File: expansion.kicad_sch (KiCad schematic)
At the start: 41 parts, among them IC10 GAL16V8, IC11 74LS367ADR, IC12 74LS367ADR, IC13 74LS368AD, IC14 74LS367ADR, IC15 74ALS30ADR, IC16 74LS245DWR, IC17 74LS367ADR, IC18 74LS139ADR, IC19 74LS153DR, IC20 74LS374DWR, IC21 74LS367ADR, IC22 74LS74ADR, J10 CARTRIDGE EDGE, J12 CARTRIDGE EDGE, J13 CARTRIDGE EDGE, J9 CARTRIDGE EDGE, SW3 DEFAULT SLOT

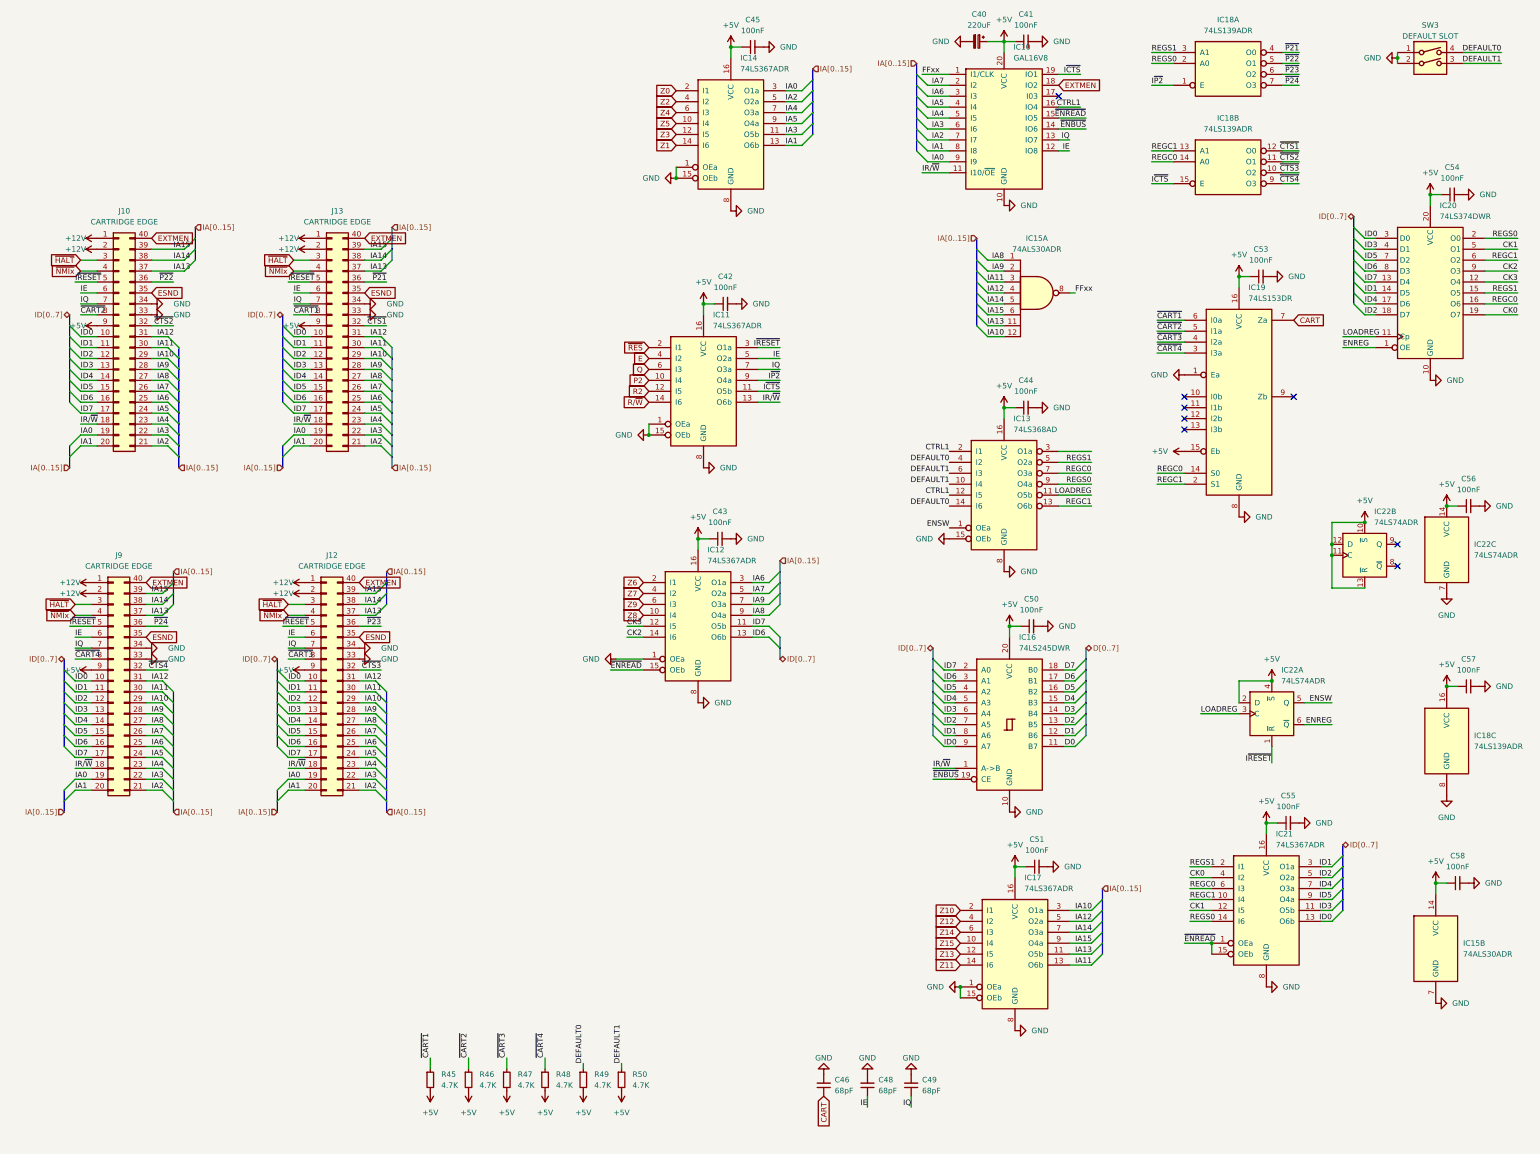
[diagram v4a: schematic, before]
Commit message: add data bus transceiver
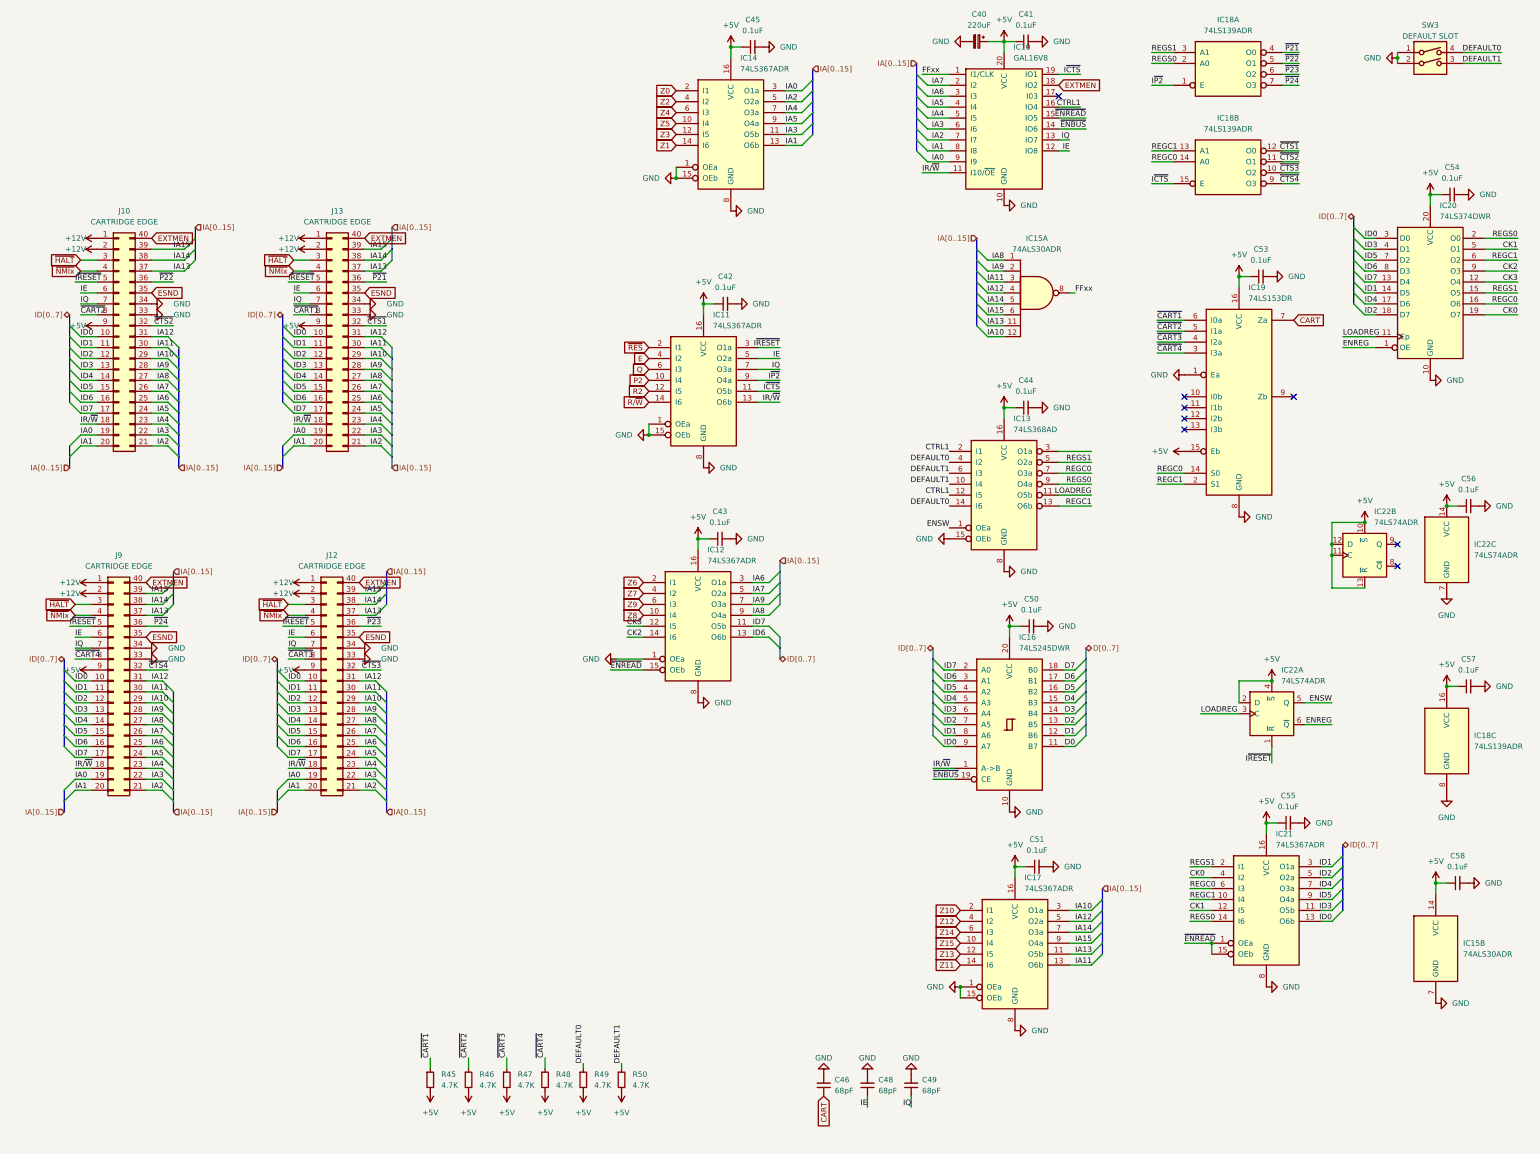
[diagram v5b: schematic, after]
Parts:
- C40: DigiKey (none) -> 732-875575345004CT-ND
- C41, C42, C43, C44, C45, C50, C51, C53, C54, C55, C56, C57, C58: value 100nF -> 0.1uF; DigiKey (none) -> 399-C0805C104K4RAC7800CT-ND
- C46, C48, C49: DigiKey (none) -> 399-C0805C680J5GAC7800CT-ND
- R45, R46, R47, R48, R49, R50: DigiKey (none) -> 541-4131-1-ND
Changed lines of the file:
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@@
 			)
 		)
-		(property "Value" "100nF"
+		(property "Value" "0.1uF"
 			(at 347.9863 201.93 90)
 			(effects
@@
 			)
 		)
+		(property "DigiKey" "399-C0805C104K4RAC7800CT-ND"
+			(at 347.98 205.74 90)
+			(effects
+				(font
+					(size 1.27 1.27)
+				)
+				(hide yes)
+			)
+		)
 		(pin "1"
 		)
@@
 			)
 		)
-		(property "Value" "100nF"
+		(property "Value" "0.1uF"
 			(at 389.8963 170.18 90)
 			(effects
@@
 			)
 		)
+		(property "DigiKey" "399-C0805C104K4RAC7800CT-ND"
+			(at 389.89 173.99 90)
+			(effects
+				(font
+					(size 1.27 1.27)
+				)
+				(hide yes)
+			)
+		)
 		(pin "1"
 		)
@@
 			)
 		)
-		(property "Value" "100nF"
+		(property "Value" "0.1uF"
 			(at 387.3563 215.9 90)
 			(effects
@@
 			)
 		)
+		(property "DigiKey" "399-C0805C104K4RAC7800CT-ND"
+			(at 387.35 219.71 90)
+			(effects
+				(font
+					(size 1.27 1.27)
+				)
+				(hide yes)
+			)
+		)
 		(pin "1"
 		)
@@
 			)
 		)
+		(property "DigiKey" "399-C0805C680J5GAC7800CT-ND"
+			(at 250.19 266.7 0)
+			(effects
+				(font
+					(size 1.27 1.27)
+				)
+				(hide yes)
+			)
+		)
 		(pin "1"
 		)
@@
 			)
 		)
-		(property "Value" "100nF"
+		(property "Value" "0.1uF"
 			(at 217.1763 81.28 90)
 			(effects
@@
 			)
 		)
+		(property "DigiKey" "399-C0805C104K4RAC7800CT-ND"
+			(at 217.17 85.09 90)
+			(effects
+				(font
+					(size 1.27 1.27)
+				)
+				(hide yes)
+			)
+		)
 		(pin "1"
 		)
@@
 			)
 		)
-		(property "Value" "100nF"
+		(property "Value" "0.1uF"
 			(at 389.8963 128.27 90)
 			(effects
@@
 			)
 		)
+		(property "DigiKey" "399-C0805C104K4RAC7800CT-ND"
+			(at 389.89 132.08 90)
+			(effects
+				(font
+					(size 1.27 1.27)
+				)
+				(hide yes)
+			)
+		)
 		(pin "1"
 		)
@@
 			)
 		)
-		(property "Value" "100nF"
+		(property "Value" "0.1uF"
 			(at 287.0263 105.41 90)
 			(effects
@@
 			)
 		)
+		(property "DigiKey" "399-C0805C104K4RAC7800CT-ND"
+			(at 287.02 109.22 90)
+			(effects
+				(font
+					(size 1.27 1.27)
+				)
+				(hide yes)
+			)
+		)
 		(pin "1"
 		)
@@
 			)
 		)
+		(property "DigiKey" "541-4131-1-ND"
+			(at 148.59 265.43 0)
+			(effects
+				(font
+					(size 1.27 1.27)
+				)
+				(hide yes)
+			)
+		)
 		(pin "1"
 		)
@@
 			)
 		)
-		(property "Value" "100nF"
+		(property "Value" "0.1uF"
 			(at 223.5263 21.59 90)
 			(effects
@@
 			)
 		)
+		(property "DigiKey" "399-C0805C104K4RAC7800CT-ND"
+			(at 223.52 25.4 90)
+			(effects
+				(font
+					(size 1.27 1.27)
+				)
+				(hide yes)
+			)
+		)
 		(pin "1"
 		)
@@
 			)
 		)
+		(property "DigiKey" "541-4131-1-ND"
+			(at 166.37 265.43 0)
+			(effects
+				(font
+					(size 1.27 1.27)
+				)
+				(hide yes)
+			)
+		)
 		(pin "1"
 		)
@@
 			)
 		)
-		(property "Value" "100nF"
+		(property "Value" "0.1uF"
 			(at 289.5663 212.09 90)
 			(effects
@@
 			)
 		)
+		(property "DigiKey" "399-C0805C104K4RAC7800CT-ND"
+			(at 289.56 215.9 90)
+			(effects
+				(font
+					(size 1.27 1.27)
+				)
+				(hide yes)
+			)
+		)
 		(pin "1"
 		)
@@
 			)
 		)
-		(property "Value" "100nF"
+		(property "Value" "0.1uF"
 			(at 287.0263 20.32 90)
 			(effects
@@
 			)
 		)
+		(property "DigiKey" "399-C0805C104K4RAC7800CT-ND"
+			(at 287.02 24.13 90)
+			(effects
+				(font
+					(size 1.27 1.27)
+				)
+				(hide yes)
+			)
+		)
 		(pin "1"
 		)
@@
 			)
 		)
-		(property "Value" "100nF"
+		(property "Value" "0.1uF"
 			(at 341.6363 74.93 90)
 			(effects
@@
 			)
 		)
+		(property "DigiKey" "399-C0805C104K4RAC7800CT-ND"
+			(at 341.63 78.74 90)
+			(effects
+				(font
+					(size 1.27 1.27)
+				)
+				(hide yes)
+			)
+		)
 		(pin "1"
 		)
@@
 			)
 		)
+		(property "DigiKey" "541-4131-1-ND"
+			(at 175.26 265.43 0)
+			(effects
+				(font
+					(size 1.27 1.27)
+				)
+				(hide yes)
+			)
+		)
 		(pin "1"
 		)
@@
 			)
 		)
+		(property "DigiKey" "732-875575345004CT-ND"
+			(at 275.59 24.13 90)
+			(effects
+				(font
+					(size 1.27 1.27)
+				)
+				(hide yes)
+			)
+		)
 		(pin "2"
 		)
@@
 			)
 		)
+		(property "DigiKey" "541-4131-1-ND"
+			(at 157.48 265.43 0)
+			(effects
+				(font
+					(size 1.27 1.27)
+				)
+				(hide yes)
+			)
+		)
 		(pin "1"
 		)
@@
 			)
 		)
+		(property "DigiKey" "399-C0805C680J5GAC7800CT-ND"
+			(at 260.35 266.7 0)
+			(effects
+				(font
+					(size 1.27 1.27)
+				)
+				(hide yes)
+			)
+		)
 		(pin "1"
 		)
@@
 			)
 		)
+		(property "DigiKey" "399-C0805C680J5GAC7800CT-ND"
+			(at 240.03 266.7 0)
+			(effects
+				(font
+					(size 1.27 1.27)
+				)
+				(hide yes)
+			)
+		)
 		(pin "1"
 		)
@@
 			)
 		)
-		(property "Value" "100nF"
+		(property "Value" "0.1uF"
 			(at 215.9063 135.89 90)
 			(effects
@@
 			)
 		)
+		(property "DigiKey" "399-C0805C104K4RAC7800CT-ND"
+			(at 215.9 139.7 90)
+			(effects
+				(font
+					(size 1.27 1.27)
+				)
+				(hide yes)
+			)
+		)
 		(pin "1"
 		)
@@
 			)
 		)
-		(property "Value" "100nF"
+		(property "Value" "0.1uF"
 			(at 386.0863 55.88 90)
 			(effects
@@
 			)
 		)
+		(property "DigiKey" "399-C0805C104K4RAC7800CT-ND"
+			(at 386.08 59.69 90)
+			(effects
+				(font
+					(size 1.27 1.27)
+				)
+				(hide yes)
+			)
+		)
 		(pin "1"
 		)
@@
 			)
 		)
+		(property "DigiKey" "541-4131-1-ND"
+			(at 193.04 265.43 0)
+			(effects
+				(font
+					(size 1.27 1.27)
+				)
+				(hide yes)
+			)
+		)
 		(pin "1"
 		)
@@
 			)
 		)
-		(property "Value" "100nF"
+		(property "Value" "0.1uF"
 			(at 288.2963 156.21 90)
 			(effects
@@
 			)
 		)
+		(property "DigiKey" "399-C0805C104K4RAC7800CT-ND"
+			(at 288.29 160.02 90)
+			(effects
+				(font
+					(size 1.27 1.27)
+				)
+				(hide yes)
+			)
+		)
 		(pin "1"
 		)
@@
 			(at 184.15 265.43 0)
 			(effects
+				(font
+					(size 1.27 1.27)
+				)
+				(hide yes)
+			)
+		)
+		(property "DigiKey" "541-4131-1-ND"
+			(at 184.15 265.43 0)
+			(effects
